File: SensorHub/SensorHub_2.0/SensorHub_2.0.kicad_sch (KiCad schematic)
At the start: 5 parts, among them J1 USB_B_Micro, U1 R7FA4E2B93CFM#AA0, U2 AP2112K-3.3

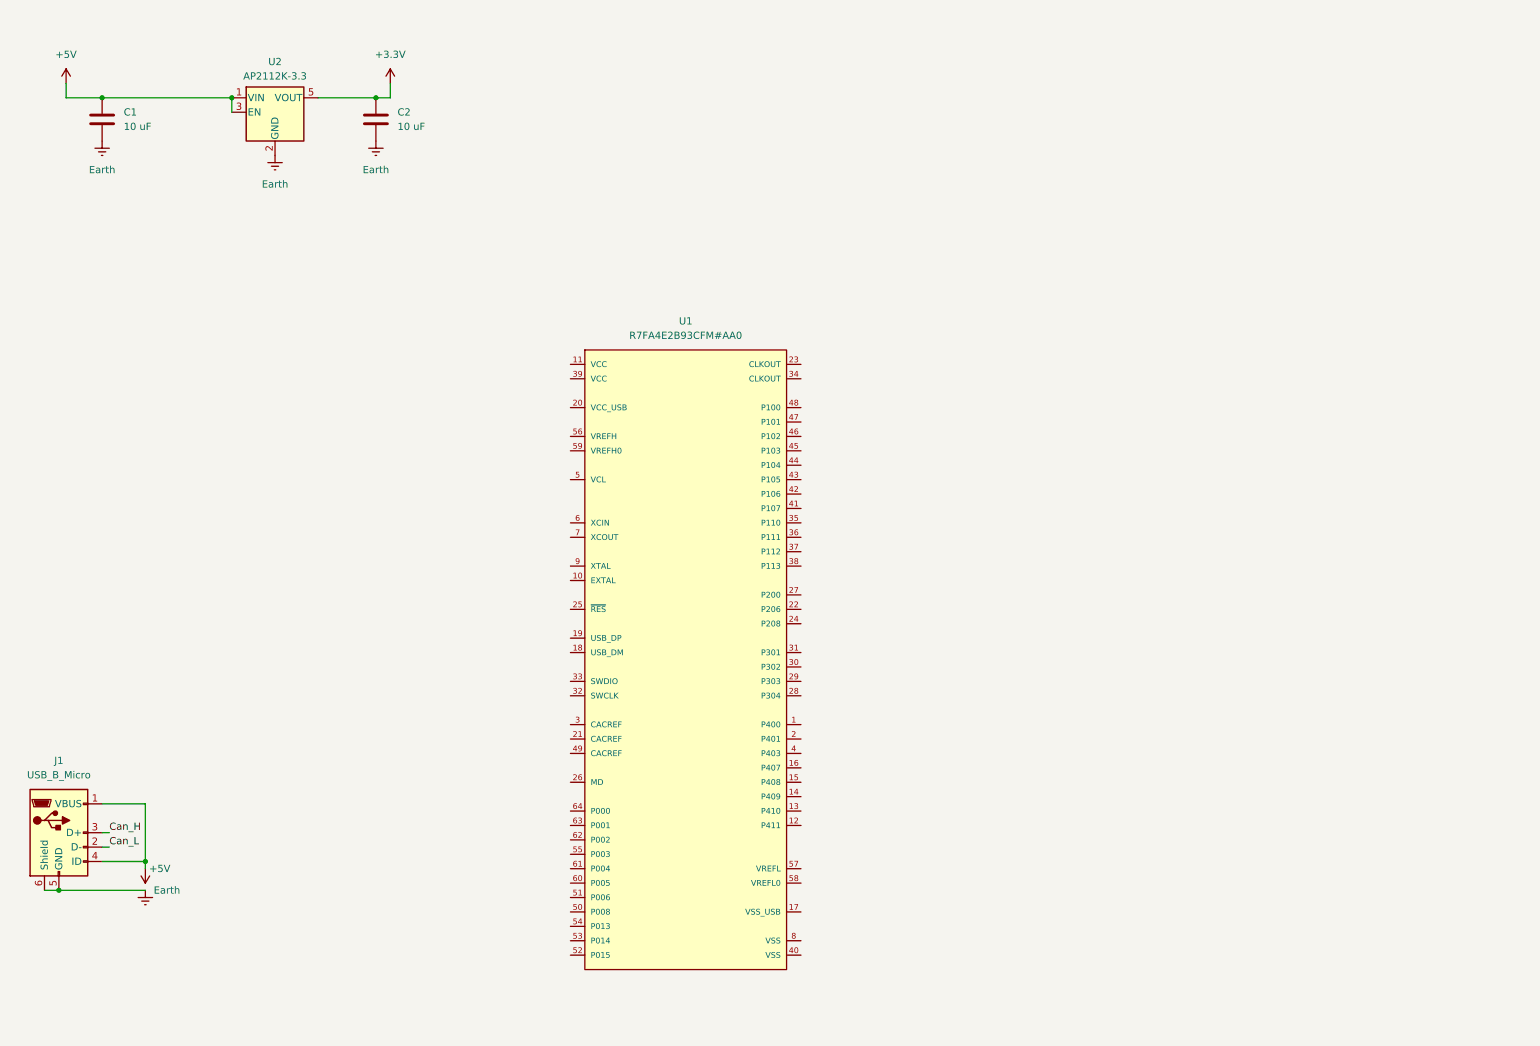
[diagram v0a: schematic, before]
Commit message: Voltage regulation
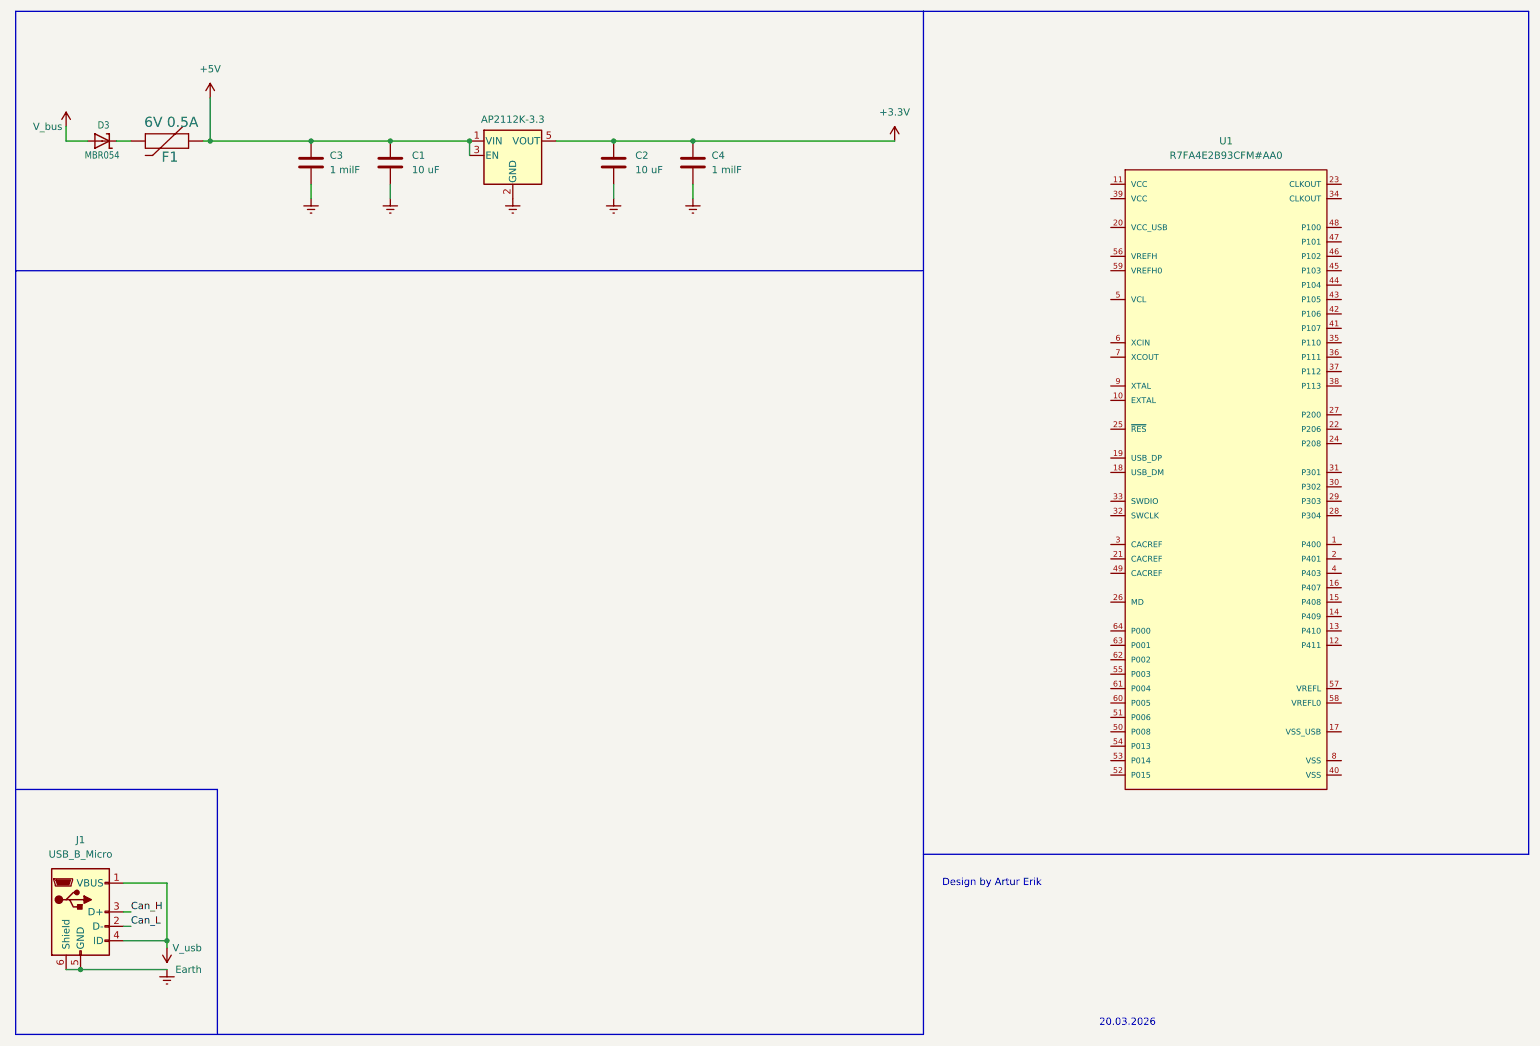
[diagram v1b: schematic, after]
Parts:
- added C3, C4: 1 milF, symbol Device:C
- added D3: MBR054, SensorHub MicroMod Carrier v1.1.0b:SOD-123, symbol SensorHub MicroMod Carrier v1.1.0b-eagle-import:DIODE-SCHOTTKYSOD-123
- added F1: 6V 0.5A, SensorHub MicroMod Carrier v1.1.0b:0805, symbol SensorHub MicroMod Carrier v1.1.0b-eagle-import:PPTC_6V500MA
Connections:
- net +3.3V: now also C4.1
- net +5V: now also C3.1, F1.1; no longer J1.1 (VBUS), J1.4 (ID)
- net Earth: now also C3.2, C4.2
- new net: D3.C, F1.2
- new net V_bus: D3.A
- new net V_usb: J1.1 (VBUS), J1.4 (ID)
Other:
- note added: "20.03.2026"
- note added: "Design by Artur Erik"
- moved on the sheet: C1, C2, J1, U1

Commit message: 1st version SensorHub
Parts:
- removed D3: MBR054, SensorHub MicroMod Carrier v1.1.0b:SOD-123, symbol SensorHub MicroMod Carrier v1.1.0b-eagle-import:DIODE-SCHOTTKYSOD-123
- added C10: 4.7 uF, Capacitor_SMD:C_0603_1608Metric, symbol Device:C
- added C11, C12, C6, C8, C9: 0.1 uF, Capacitor_SMD:C_0603_1608Metric, symbol Device:C
- added C5, C7: 1 uF, Capacitor_SMD:C_0603_1608Metric, symbol Device:C
- added D1, D2: LED, LED_SMD:LED_0402_1005Metric, symbol Device:LED
- added D3: 1N4148WT, Diode_SMD:D_SOD-523, symbol Diode:1N4148WT
- added J2: Conn_01x03, Connector_PinHeader_2.54mm:PinHeader_1x03_P2.54mm_Vertical, symbol Connector_Generic:Conn_01x03
- added J3: Conn_01x05, Connector_PinHeader_2.54mm:PinHeader_1x05_P2.54mm_Vertical, symbol Connector_Generic:Conn_01x05
- added JP1, JP2, JP3: SolderJumper_3_Open, Jumper:SolderJumper-3_P1.3mm_Open_RoundedPad1.0x1.5mm, symbol Jumper:SolderJumper_3_Open
- added R1: 15 K, Resistor_SMD:R_0201_0603Metric, symbol Device:R
- added R10, R4, R9: 4.7 K, Resistor_SMD:R_0201_0603Metric, symbol Device:R
- added R11: 1 K, Resistor_SMD:R_0201_0603Metric, symbol Device:R
- added R2: 30 K, Resistor_SMD:R_0201_0603Metric, symbol Device:R
- added R3, R8: 1.33 K, Resistor_SMD:R_0201_0603Metric, symbol Device:R
- added R5: 1.5 K, Resistor_SMD:R_0201_0603Metric, symbol Device:R
- added R6: 10 K, Resistor_SMD:R_0201_0603Metric, symbol Device:R
- added R7: ~, Resistor_SMD:R_0201_0603Metric, symbol Device:R
- added S1: Reset, Library:Button_Mini_2.5x1.7mm, symbol SensorHub MicroMod Carrier v1.1.0b-eagle-import:MOMENTARY-SWITCH-SPST-SMD-5.2-T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
- added S2: Boot, Library:Button_Mini_2.5x1.7mm, symbol SensorHub MicroMod Carrier v1.1.0b-eagle-import:MOMENTARY-SWITCH-SPST-SMD-5.2-T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
- added U3: TJA1051TK-3, Package_SON:HVSON-8-1EP_3x3mm_P0.65mm_EP1.6x2.4mm, symbol Interface_CAN_LIN:TJA1051TK-3
- added U4: BMI270, BMI270:XDCR_BMI270, symbol BMI270:BMI270
- C1, C2, C3, C4: footprint (none) -> Capacitor_SMD:C_0603_1608Metric
- J1: footprint (none) -> Connector_USB:USB_Micro-B_Molex-105017-0001
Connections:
- net Earth is gone; now on net GND: C1.2, C2.2, C3.2, C4.2, J1.5 (GND), J1.6 (Shield), U2.2 (GND)
- net +3.3V: now also U1.11 (VCC), U1.39 (VCC), U1.56 (VREFH), U1.59 (VREFH0), C8.1, C9.1, J2.3 (Pin_3), J3.3 (Pin_3), R10.1, R4.1, R6.1, R9.1, U3.5 (VIO), U4.12 (CSB), U4.5 (VDDIO), U4.8 (VDD)
- net +5V: now also C6.1, J3.1 (Pin_1), U3.3 (VCC)
- net Can_H: now also JP1.1 (A), U3.7 (CANH); no longer J1.3 (D+)
- net Can_L: now also JP2.1 (A), U3.6 (CANL); no longer J1.2 (D-)
- net V_usb: now also JP3.2 (C)
- net Sleep: now reaches U1.1 (P400)
- net Sleep: now also U3.8 (S)
- net SCX: now reaches U1.15 (P408)
- net SCX: now also J3.4 (Pin_4), R9.2, U4.13 (SCX)
- net SDX: now reaches U1.16 (P407)
- net SDX: now also J3.5 (Pin_5), R10.2, U4.14 (SDX)
- net GND: now reaches U1.17 (VSS_USB)
- net GND: now also U1.40 (VSS), U1.8 (VSS), C10.2, C11.2, C12.2, C5.1, C6.2, C7.2, C8.2, C9.2, D1.1 (K), D2.1 (K), J2.2 (Pin_2), J3.2 (Pin_2), R2.2, R5.2, S1.1, S1.2 (1), U3.2 (GND), U3.9 (GND), U4.1 (SDO), U4.6 (GNDIO), U4.7 (GND)
- net USB_DM: now reaches U1.18 (USB_DM)
- net USB_DM: now also JP2.3 (B)
- net USB_DP: now reaches U1.19 (USB_DP)
- net USB_DP: now also JP1.3 (B)
- net TXD: now reaches U1.2 (P401)
- net TXD: now also U3.1 (TXD)
- net V_USB_Mic: now reaches U1.20 (VCC_USB)
- net V_USB_Mic: now also C11.1, C5.2, R1.1, R2.1
- net RES: now reaches U1.25 (~{RES})
- net RES: now also C7.1, R4.2, S1.3 (2), S1.4 (2)
- net Boot: now reaches U1.26 (MD)
- net Boot: now also R6.2, S2.3 (2), S2.4 (2)
- net RXD: now reaches U1.3 (CACREF)
- net RXD: now also U3.4 (RXD)
- net P112: now reaches U1.37 (P112)
- net P112: now also R3.1
- net P113: now reaches U1.38 (P113)
- net P113: now also R8.1
- net INT1: now reaches U1.44 (P104)
- net INT1: now also U4.4 (INT1)
- net VCL: now reaches U1.5 (VCL)
- net VCL: now also C10.1
- net P000: now reaches U1.64 (P000)
- net P000: now also R11.2
- net at F1.2: now also D3.1 (K)
- new net: R5.1, S2.1, S2.2 (1)
- new net: D2.2 (A), R8.2
- new net: D1.2 (A), R3.2
- new net Analog: C12.1, J2.1 (Pin_1), R11.1
- new net USB_D+: J1.3 (D+), JP1.2 (C), R7.2
- new net USB_D-: J1.2 (D-), JP2.2 (C), R7.1
- new net V_Bus: D3.2 (A), JP3.1 (A)
- new net V_USB_Mic_inp: JP3.3 (B), R1.2
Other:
- note added: "Analog"
- note added: "CAN transceiver"
- note added: "I2C"
- note added: "IMU"
- note added: "Pull-Up (optional)"
- note added: "Reset/Boot"
- note added: "USB"
- note added: "USB/CAN Jumpers"
- note added: "User LED"
- moved on the sheet: C1, C2, C3, C4, J1, U1

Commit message: MYRGM080200C41RA
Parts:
- removed F1: 6V 0.5A, SensorHub MicroMod Carrier v1.1.0b:0805, symbol SensorHub MicroMod Carrier v1.1.0b-eagle-import:PPTC_6V500MA
- removed J1: USB_B_Micro, Connector_USB:USB_Micro-B_Molex-105017-0001, symbol Connector:USB_B_Micro
- removed JP1, JP2, JP3: SolderJumper_3_Open, Jumper:SolderJumper-3_P1.3mm_Open_RoundedPad1.0x1.5mm, symbol Jumper:SolderJumper_3_Open
- removed R7: ~, Resistor_SMD:R_0201_0603Metric, symbol Device:R
- removed U2: AP2112K-3.3, Package_TO_SOT_SMD:SOT-23-5, symbol Regulator_Linear:AP2112K-3.3
- added C13, C14, C15: 0.1 uF, Capacitor_SMD:C_0603_1608Metric, symbol Device:C
- added F1: 6V 0.5A, Fuse:Fuse_1206_3216Metric_Pad1.42x1.75mm_HandSolder, symbol Device:Fuse
- added J4: USB_C_Receptacle, Connector_USB:USB_C_Receptacle_Molex_105450-0101, symbol Connector:USB_C_Receptacle
- added R12: 15 K, Resistor_SMD:R_0201_0603Metric, symbol Device:R
- added R13, R14: ~, Resistor_SMD:R_0201_0603Metric, symbol Device:R
- added U2: MYRGM080200C41RA, MYRGM080200C41RA:MURATA_MYRGM080200C41RA_0, symbol MYRGM080200C41RA:MYRGM080200C41RA
- C1, C2: value 10 uF -> 10V/22uF
- C3: value 1 milF -> 330 pF
- C4: value 1 milF -> 50 nF
- C5: value 1 uF -> 0.1 uF
- C6: value 0.1 uF -> 16V/1uF
- R1: value 15 K -> 10 K
- R2: value 30 K -> 47 K
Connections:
- net V_USB_Mic_inp is gone; now on net GND: R1.2
- net +3.3V: now also C11.1, C3.1, C5.1, J2.2 (Pin_2), R2.1, U1.20 (VCC_USB), C13.1, C14.1, C15.1, U2.11 (L2); no longer C4.1, J2.3 (Pin_3)
- net +5V: now also F1.1, U2.7 (AVIN), U2.9 (PVIN); no longer C3.1
- net Can_H: now also J4.A10 (RX2-), J4.B10 (RX1-), R13.2
- net Can_L: now also J4.A11 (RX2+), J4.B11 (RX1+), R14.2
- net GND: now also C5.2, J2.3 (Pin_3), C13.2, C14.2, C15.2, J4.A1 (GND), J4.A12 (GND), J4.B1 (GND), J4.B12 (GND), J4.S1 (SHIELD), R12.2, U2.8 (GND); no longer C3.2, C5.1, J2.2 (Pin_2), R2.2
- net RES: now also J4.A3 (TX1-), J4.B3 (TX2-)
- net Sleep: now also R1.1, J4.A8 (SBU1), J4.B8 (SBU2), U2.6 (CE); no longer U1.1 (P400), U3.8 (S)
- net USB_DM: now also J4.A7 (D-), J4.B7 (D-)
- net USB_DP: now also J4.A6 (D+), J4.B6 (D+)
- net V_Bus: now also J4.A4 (VBUS), J4.A9 (VBUS), J4.B4 (VBUS), J4.B9 (VBUS)
- net P109 / TXD9: now reaches U1.34 (CLKOUT)
- net P109 / TXD9: now also J4.A2 (TX1+), J4.B2 (TX2+)
- net at D3.1 (K): now also F1.2
- removed net V_USB_Mic: C11.1, C5.2, R1.1, R2.1, U1.20 (VCC_USB)
- new net: C4.1, R13.1, R14.1
- new net FB: C3.2, R12.1, R2.2, U2.5 (FB)
- new net LX: U2.10 (L1), U2.2 (1_LX), U2.3 (2_LX)
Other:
- note removed: "USB"
- note removed: "USB/CAN Jumpers"
- moved on the sheet: C10, C11, D3, R10, R9, U3

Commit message: ASCODV-24.000MHZ-LR-T3
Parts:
- added C16: 0.1 uF, Capacitor_SMD:C_0603_1608Metric, symbol Device:C
- added U5: ASCODV-24.000MHZ-LR-T3, Library:ASCODV-24.000MHZ-LR-T3, symbol Library:ASCODV-24.000MHZ-LR-T3
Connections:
- net +3.3V: now also C16.1, U5.1 (Tri-State), U5.3 (Vdd)
- net GND: now also C16.2, U5.4 (GND)
- net EXTAL: now reaches U1.10 (EXTAL)
- net EXTAL: now also U5.2 (Output)
